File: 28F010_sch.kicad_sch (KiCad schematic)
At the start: 5 parts

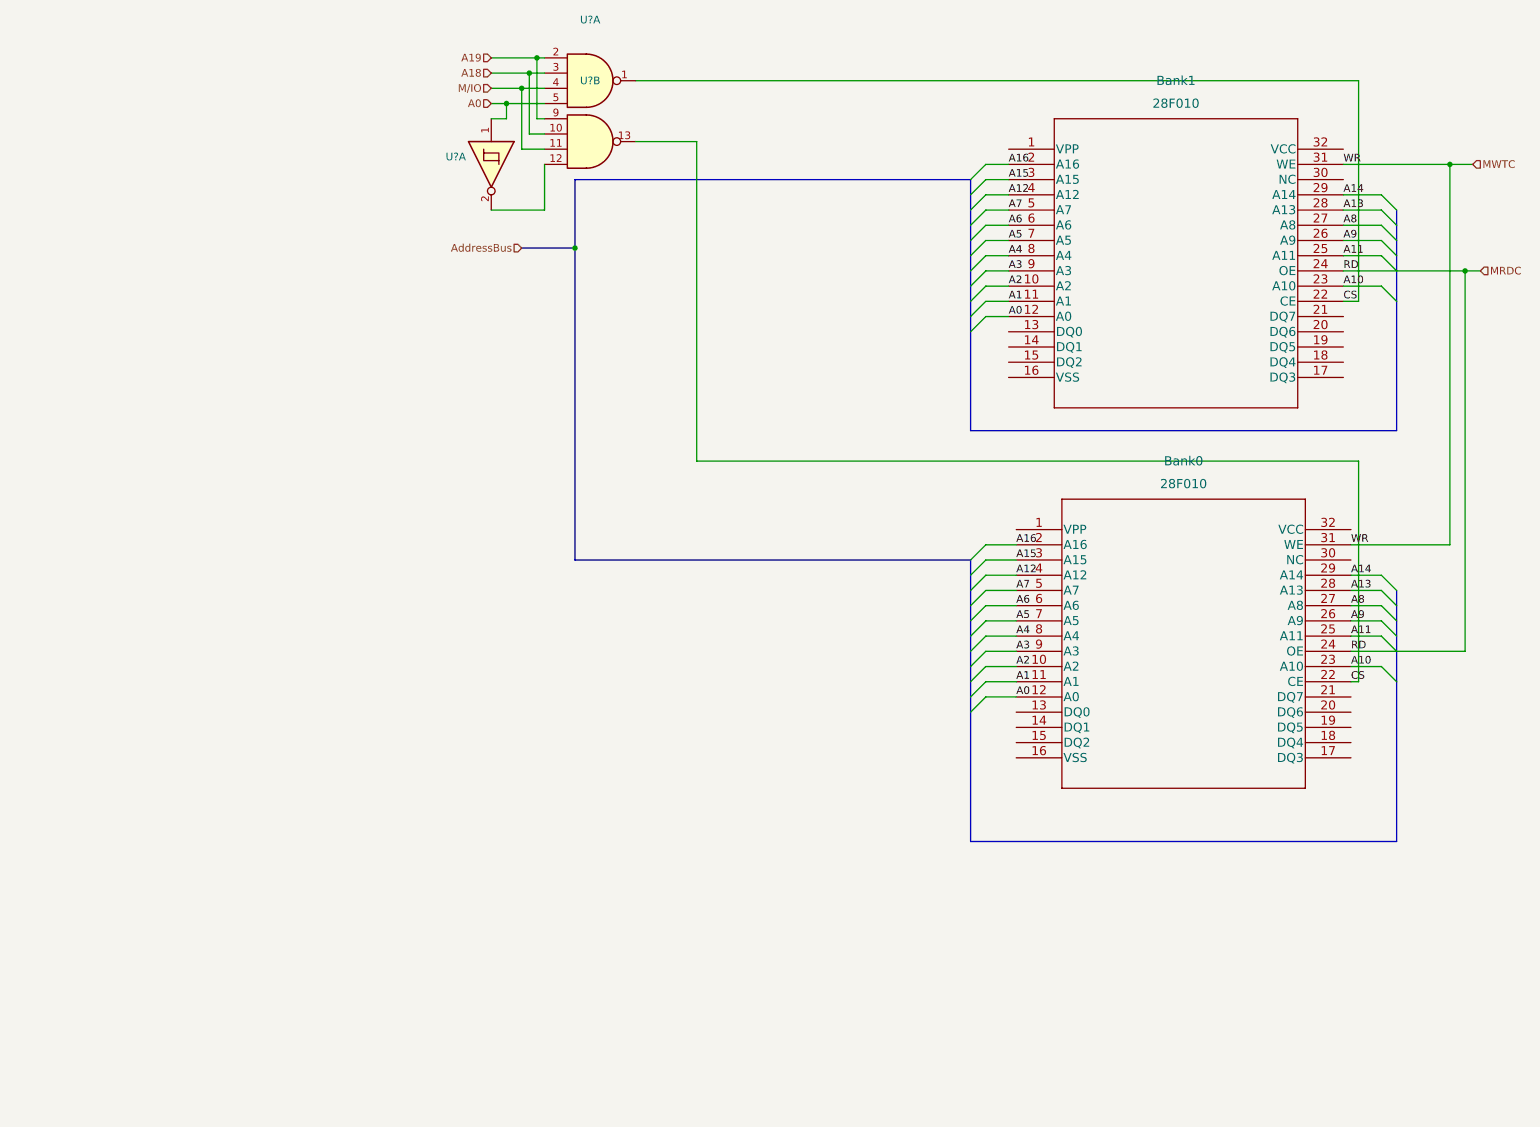
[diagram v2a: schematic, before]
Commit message: File Updates (RAM wired)
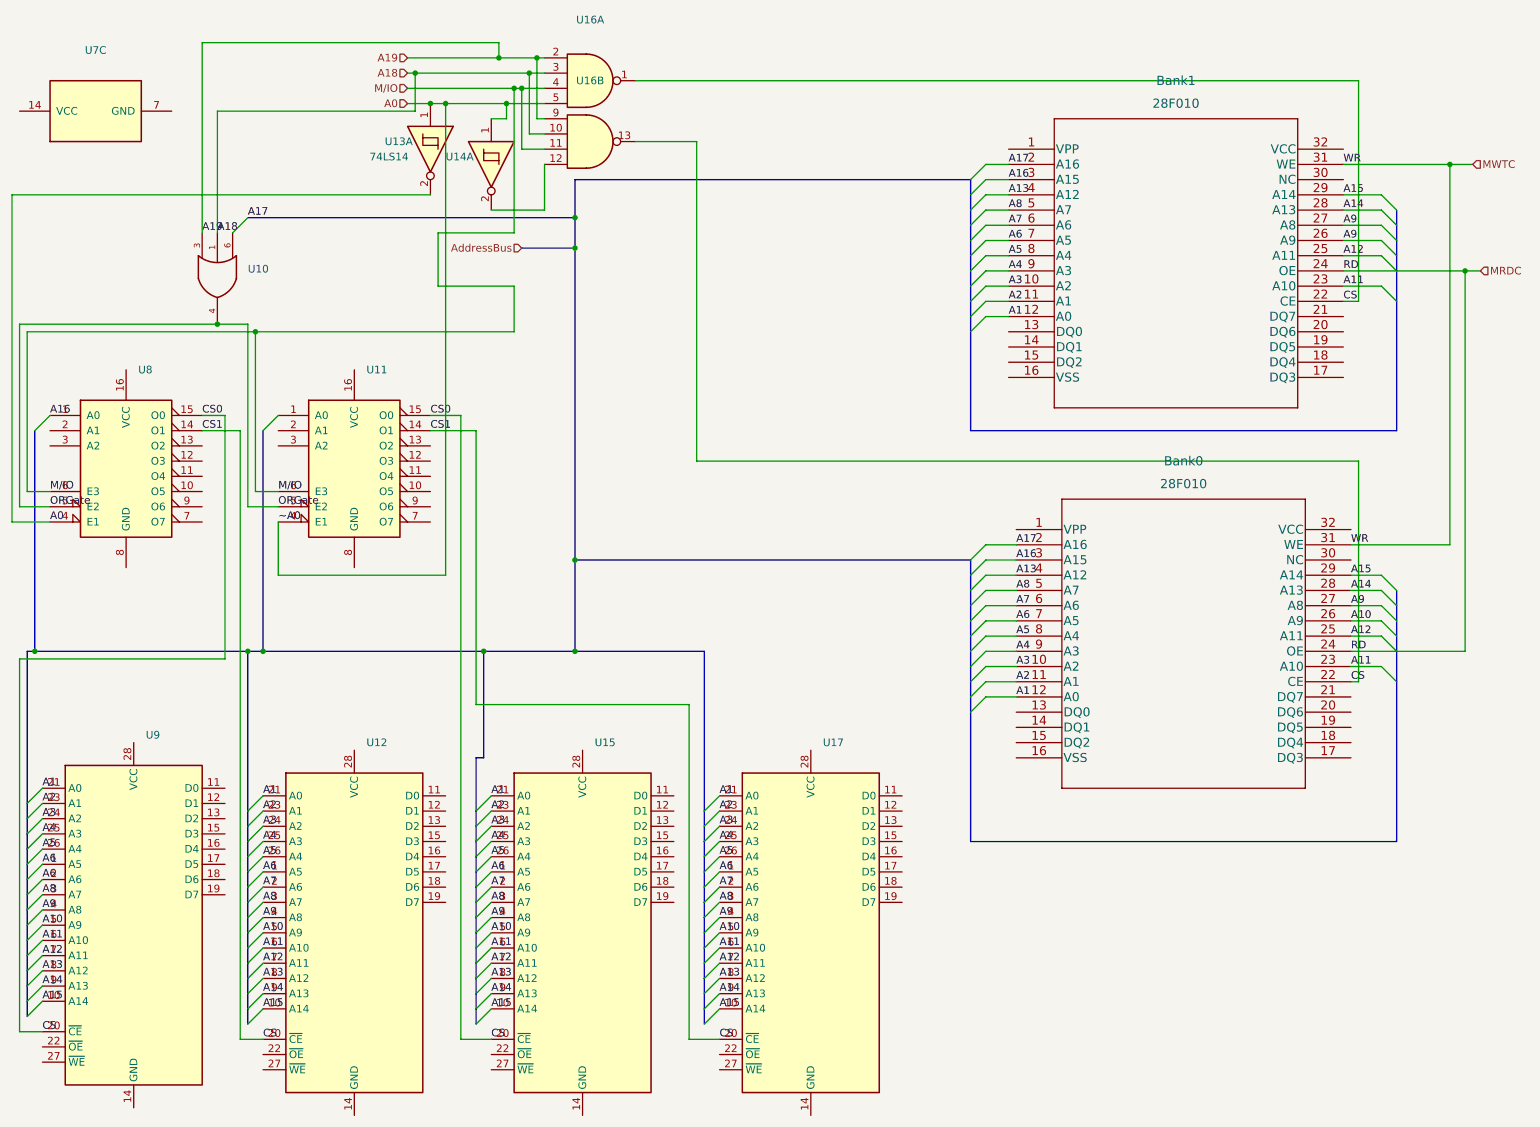
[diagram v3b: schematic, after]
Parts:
- added U10: (no value), symbol 74xGxx:74LVC1G332
- added U11, U8: (no value), symbol 74xx:74LS138
- added U12, U15, U17, U9: (no value), symbol Memory_RAM:CY7C199
- added U13: 74LS14, symbol 74xx:74LS14
- added U7: (no value), symbol 74xx:74LS13
- gave numbers to parts that had none: 2
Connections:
- net A0: now also U11.4 (E1), U13.1, U13.2, U8.4 (E1); no longer Bank0.12 (A0), Bank1.12 (A0)
- net A1: now also Bank0.12 (A0), Bank1.12 (A0), U12.21 (A0), U15.21 (A0), U17.21 (A0), U9.21 (A0); no longer Bank0.11 (A1), Bank1.11 (A1)
- net A10: now also Bank0.26 (A9), U12.5 (A9), U15.5 (A9), U17.5 (A9), U9.5 (A9); no longer Bank0.23 (A10), Bank1.23 (A10)
- net A11: now also Bank0.23 (A10), Bank1.23 (A10), U12.6 (A10), U15.6 (A10), U17.6 (A10), U9.6 (A10); no longer Bank0.25 (A11), Bank1.25 (A11)
- net A12: now also Bank0.25 (A11), Bank1.25 (A11), U12.7 (A11), U15.7 (A11), U17.7 (A11), U9.7 (A11); no longer Bank0.4 (A12), Bank1.4 (A12)
- net A13: now also Bank0.4 (A12), Bank1.4 (A12), U12.8 (A12), U15.8 (A12), U17.8 (A12), U9.8 (A12); no longer Bank0.28 (A13), Bank1.28 (A13)
- net A14: now also Bank0.28 (A13), Bank1.28 (A13), U12.9 (A13), U15.9 (A13), U17.9 (A13), U9.9 (A13); no longer Bank0.29 (A14), Bank1.29 (A14)
- net A15: now also Bank0.29 (A14), Bank1.29 (A14), U12.10 (A14), U15.10 (A14), U17.10 (A14), U9.10 (A14); no longer Bank0.3 (A15), Bank1.3 (A15)
- net A16: now also Bank0.3 (A15), Bank1.3 (A15), U8.1 (A0); no longer Bank0.2 (A16), Bank1.2 (A16)
- net A18: now also U10.1
- net A19: now also U10.3
- net A2: now also Bank0.11 (A1), Bank1.11 (A1), U12.23 (A1), U15.23 (A1), U17.23 (A1), U9.23 (A1); no longer Bank0.10 (A2), Bank1.10 (A2)
- net A3: now also Bank0.10 (A2), Bank1.10 (A2), U12.24 (A2), U15.24 (A2), U17.24 (A2), U9.24 (A2); no longer Bank0.9 (A3), Bank1.9 (A3)
- net A4: now also Bank0.9 (A3), Bank1.9 (A3), U12.25 (A3), U15.25 (A3), U17.25 (A3), U9.25 (A3); no longer Bank0.8 (A4), Bank1.8 (A4)
- net A5: now also Bank0.8 (A4), Bank1.8 (A4), U12.26 (A4), U15.26 (A4), U17.26 (A4), U9.26 (A4); no longer Bank0.7 (A5), Bank1.7 (A5)
- net A6: now also Bank0.7 (A5), Bank1.7 (A5), U12.1 (A5), U15.1 (A5), U17.1 (A5), U9.1 (A5), U9.2 (A6); no longer Bank0.6 (A6), Bank1.6 (A6)
- net A7: now also Bank0.6 (A6), Bank1.6 (A6), U12.2 (A6), U15.2 (A6), U17.2 (A6); no longer Bank0.5 (A7), Bank1.5 (A7)
- net A8: now also Bank0.5 (A7), Bank1.5 (A7), U12.3 (A7), U15.3 (A7), U17.3 (A7), U9.3 (A7); no longer Bank0.27 (A8), Bank1.27 (A8)
- net A9: now also Bank0.27 (A8), Bank1.27 (A8), U12.4 (A8), U15.4 (A8), U17.4 (A8), U9.4 (A8); no longer Bank0.26 (A9)
- net CS: now also U11.14 (O1), U11.15 (O0), U12.20 (~{CE}), U15.20 (~{CE}), U17.20 (~{CE}), U8.14 (O1), U8.15 (O0), U9.20 (~{CE})
- net M/IO: now also U11.6 (E3), U8.6 (E3)
- new net A17: Bank0.2 (A16), Bank1.2 (A16)
- new net GND: U10.2 (GND)
- new net ORGate: U10.4, U11.5 (E2), U8.5 (E2)
- new net VCC: U10.5 (VCC)

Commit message: Added new schematic sheets for INTR components
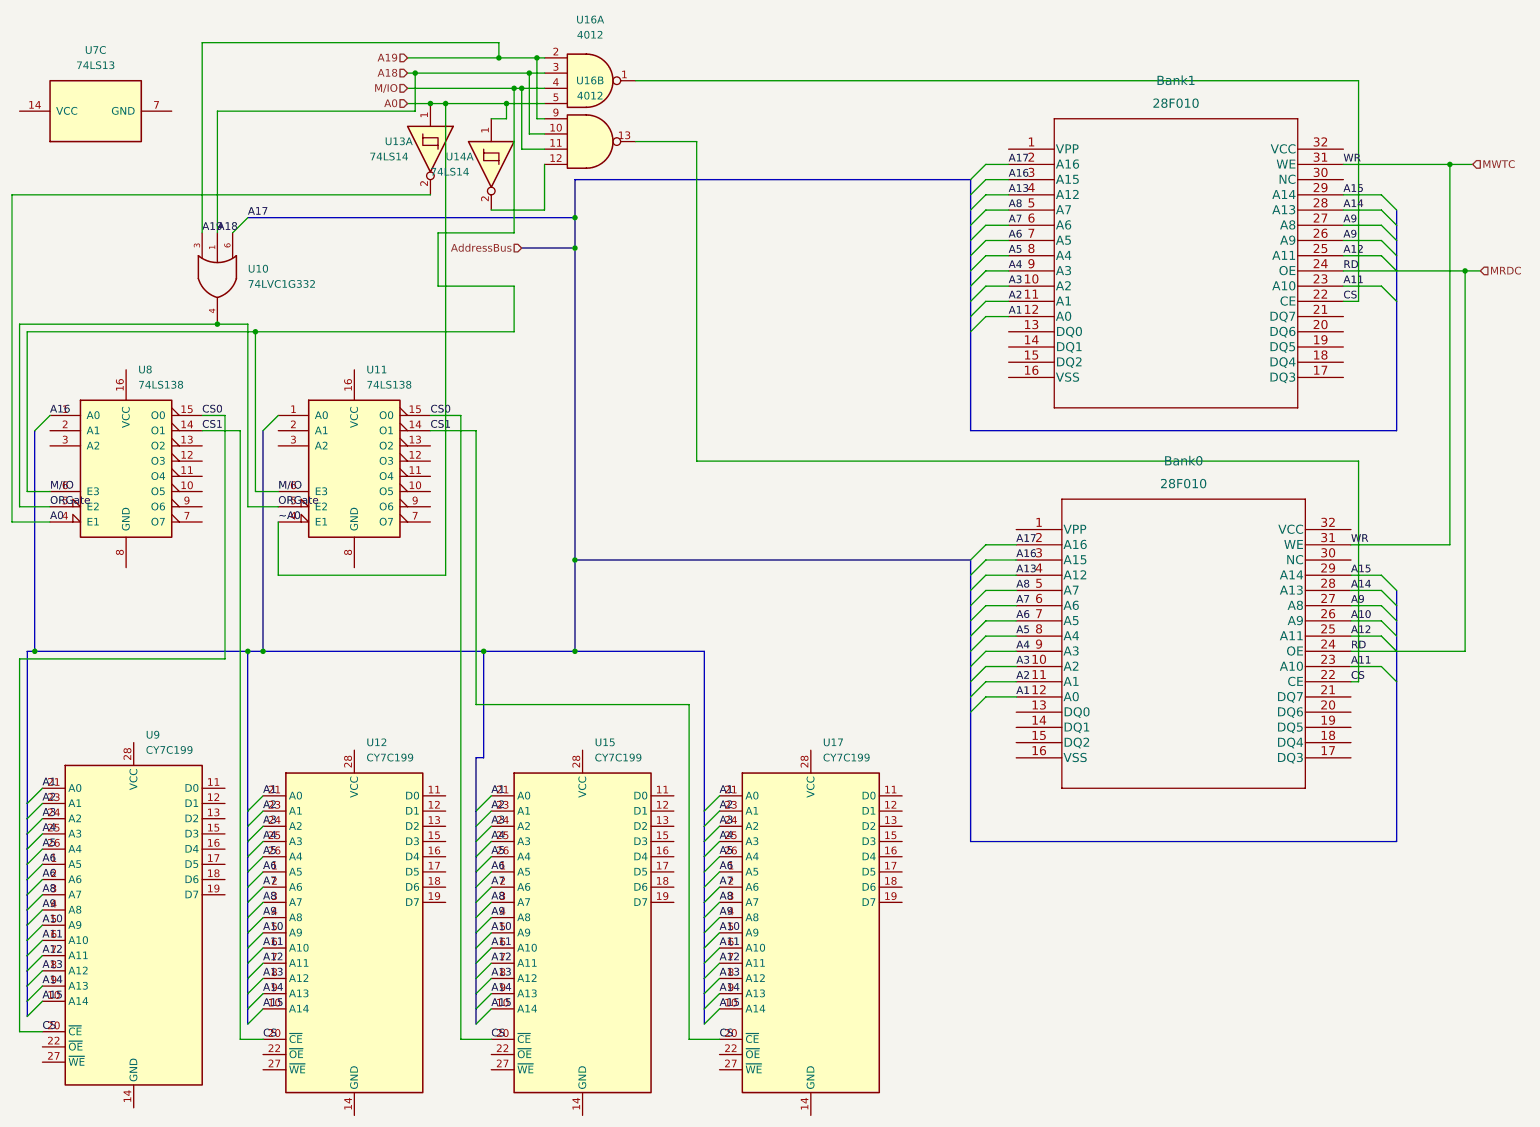
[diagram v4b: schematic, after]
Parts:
- U10: value (none) -> 74LVC1G332
- U11, U8: value (none) -> 74LS138
- U12, U15, U17, U9: value (none) -> CY7C199
- U14: value (none) -> 74LS14
- U16: value (none) -> 4012
- U7: value (none) -> 74LS13
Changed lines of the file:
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@@
     (in_bom yes) (on_board yes) (fields_autoplaced)
     (property "Reference" "U7" (id 0) (at 29.21 13.97 90))
-    (property "Value" "" (id 1) (at 29.21 16.51 90))
+    (property "Value" "74LS13" (id 1) (at 29.21 16.51 90))
     (property "Footprint" "" (id 2) (at 29.21 24.13 0)
       (effects (font (size 1.27 1.27)) hide)
@@
       (effects (font (size 1.27 1.27)) (justify left))
     )
-    (property "Value" "" (id 1) (at 74.4094 69.85 0)
+    (property "Value" "74LS138" (id 1) (at 74.4094 69.85 0)
       (effects (font (size 1.27 1.27)) (justify left))
     )
@@
       (effects (font (size 1.27 1.27)) (justify left))
     )
-    (property "Value" "" (id 1) (at 112.5094 132.08 0)
+    (property "Value" "CY7C199" (id 1) (at 112.5094 132.08 0)
       (effects (font (size 1.27 1.27)) (justify left))
     )
@@
       (effects (font (size 1.27 1.27)) (justify left))
     )
-    (property "Value" "" (id 1) (at 36.3094 69.85 0)
+    (property "Value" "74LS138" (id 1) (at 36.3094 69.85 0)
       (effects (font (size 1.27 1.27)) (justify left))
     )
@@
     (in_bom yes) (on_board yes) (fields_autoplaced)
     (property "Reference" "U16" (id 0) (at 111.76 8.89 0))
-    (property "Value" "" (id 1) (at 111.76 11.43 0))
+    (property "Value" "4012" (id 1) (at 111.76 11.43 0))
     (property "Footprint" "" (id 2) (at 111.76 19.05 0)
       (effects (font (size 1.27 1.27)) hide)
@@
       (effects (font (size 1.27 1.27)) (justify left))
     )
-    (property "Value" "" (id 1) (at 37.5794 130.81 0)
+    (property "Value" "CY7C199" (id 1) (at 37.5794 130.81 0)
       (effects (font (size 1.27 1.27)) (justify left))
     )
@@
       (effects (font (size 1.27 1.27)) (justify left))
     )
-    (property "Value" "" (id 1) (at 54.61 53.0224 90)
+    (property "Value" "74LVC1G332" (id 1) (at 54.61 53.0224 90)
       (effects (font (size 1.27 1.27)) (justify left))
     )
@@
       (effects (font (size 1.27 1.27)) (justify left))
     )
-    (property "Value" "" (id 1) (at 150.6094 132.08 0)
+    (property "Value" "CY7C199" (id 1) (at 150.6094 132.08 0)
       (effects (font (size 1.27 1.27)) (justify left))
     )
@@
       (effects (font (size 1.27 1.27)) (justify left))
     )
-    (property "Value" "" (id 1) (at 85.09 34.29 90)
+    (property "Value" "74LS14" (id 1) (at 85.09 34.29 90)
       (effects (font (size 1.27 1.27)) (justify left))
     )
@@
     (in_bom yes) (on_board yes) (fields_autoplaced)
     (property "Reference" "U16" (id 0) (at 111.76 19.05 0))
-    (property "Value" "" (id 1) (at 111.76 21.59 0))
+    (property "Value" "4012" (id 1) (at 111.76 21.59 0))
     (property "Footprint" "" (id 2) (at 111.76 29.21 0)
       (effects (font (size 1.27 1.27)) hide)
@@
       (effects (font (size 1.27 1.27)) (justify left))
     )
-    (property "Value" "" (id 1) (at 74.4094 132.08 0)
-      (effects (font (size 1.27 1.27)) (justify left))
-    )
+    (property "Value" "CY7C199" (id 1) (at 74.4094 132.08 0)
+      (effects (font (size 1.27 1.27)) (justify left))
+    )

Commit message: Wired the UART to the 8259A
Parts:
- Bank0, Bank1: footprint 28F010 -> (none)
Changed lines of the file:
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@@
       (effects (font (size 1.524 1.524)))
     )
-    (property "Footprint" "28F010" (id 2) (at 210.82 87.884 0)
+    (property "Footprint" "" (id 2) (at 210.82 87.884 0)
       (effects (font (size 1.524 1.524)) hide)
     )
@@
       (effects (font (size 1.524 1.524)))
     )
-    (property "Footprint" "28F010" (id 2) (at 209.55 24.384 0)
+    (property "Footprint" "" (id 2) (at 209.55 24.384 0)
       (effects (font (size 1.524 1.524)) hide)
     )
